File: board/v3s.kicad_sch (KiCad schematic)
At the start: 0 parts

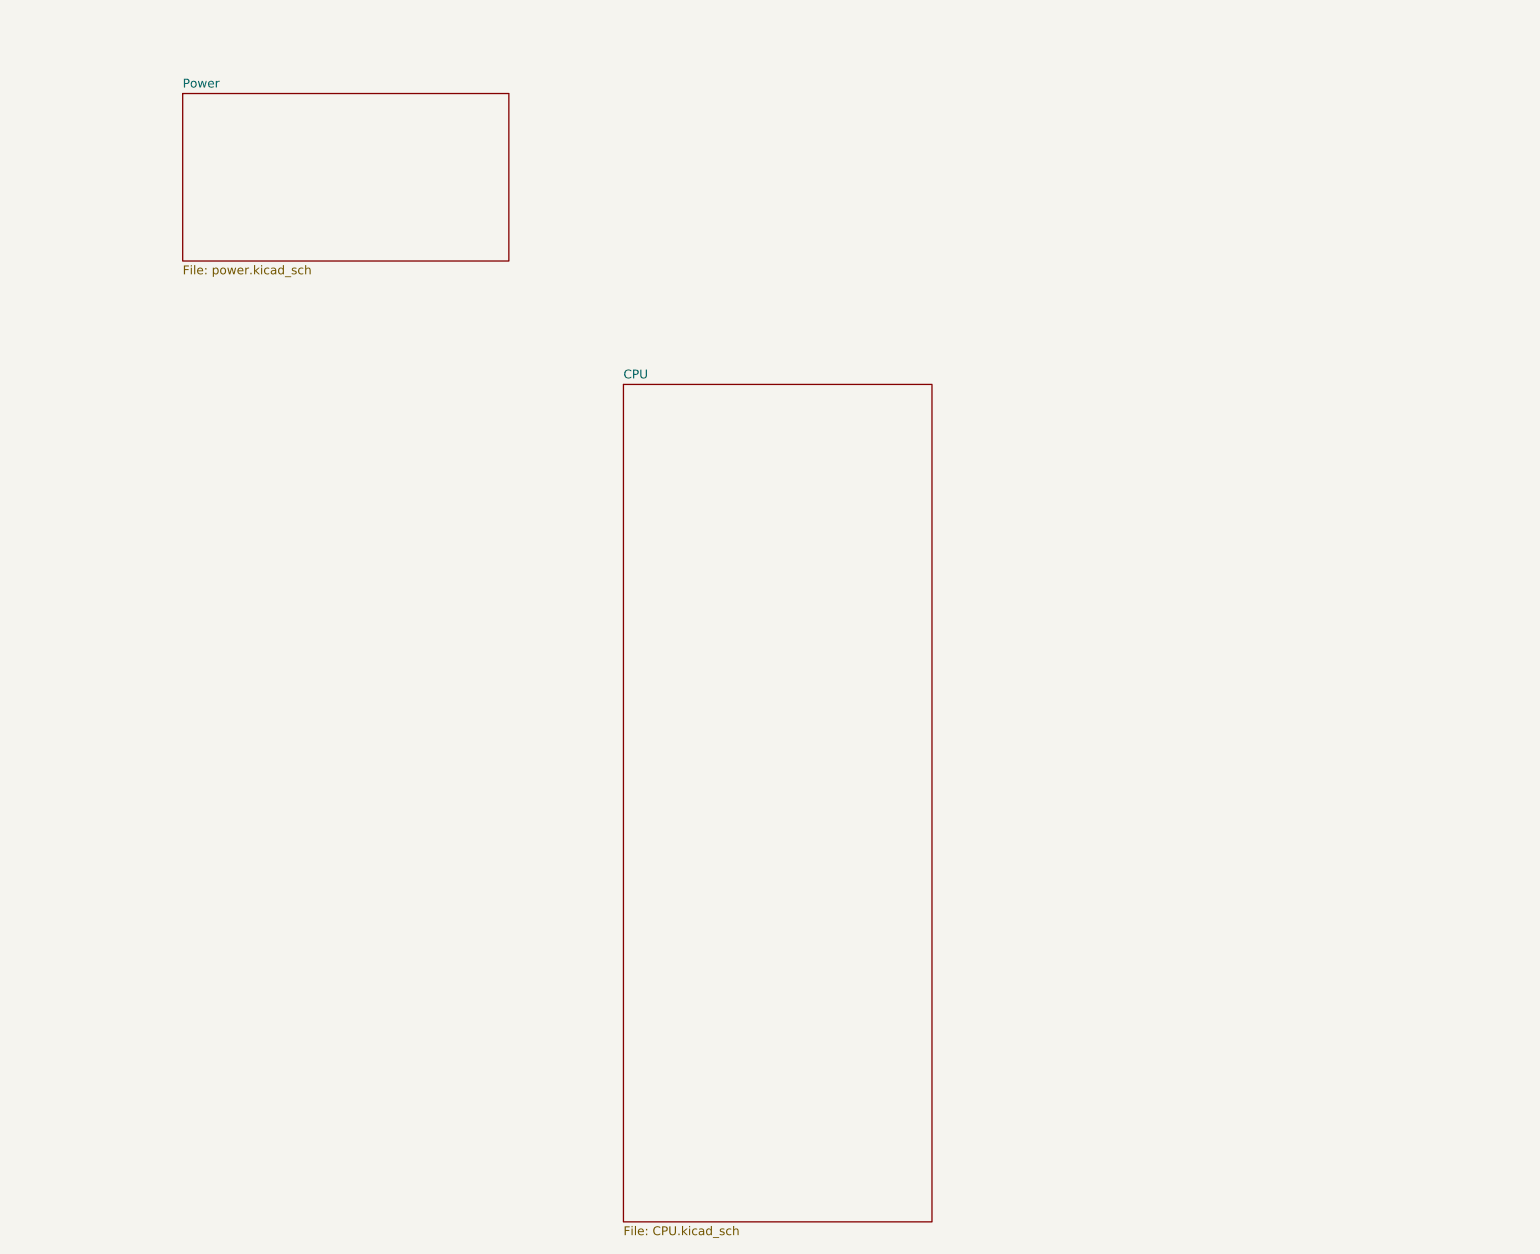
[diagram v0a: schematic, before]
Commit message: schematic update, choose components, creeate footprints
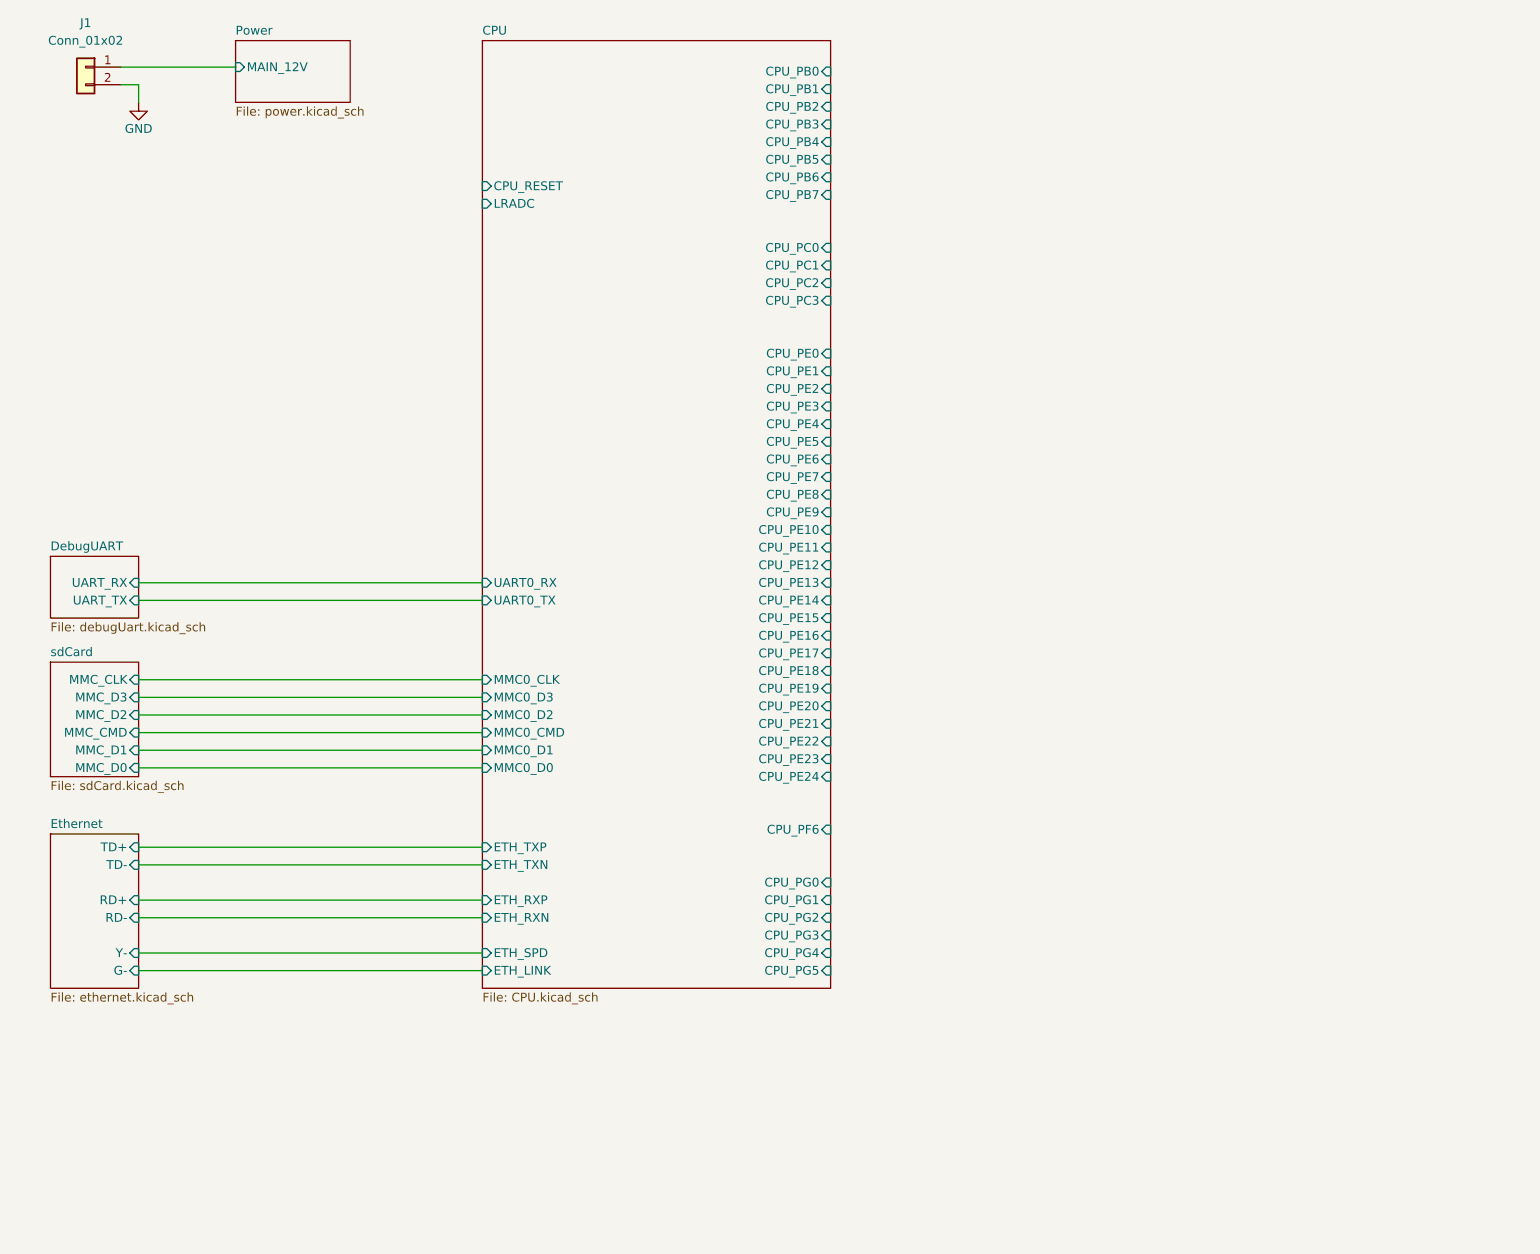
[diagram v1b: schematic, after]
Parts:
- added J1: Conn_01x02, Connector_JST:JST_PH_B2B-PH-K_1x02_P2.00mm_Vertical, symbol Connector_Generic:Conn_01x02
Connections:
- new net GND: J1.2 (Pin_2)
- new net Power/MAIN_12V: J1.1 (Pin_1)
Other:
- added sheet DebugUART (debugUart.kicad_sch)
- added sheet Ethernet (ethernet.kicad_sch)
- added sheet sdCard (sdCard.kicad_sch)
- sheet CPU ports: added CPU_PB0, CPU_PB1, CPU_PB2, CPU_PB3, CPU_PB4, CPU_PB5, CPU_PB6, CPU_PB7, CPU_PC0, CPU_PC1, CPU_PC2, CPU_PC3, CPU_PE0, CPU_PE1, CPU_PE10, CPU_PE11, CPU_PE12, CPU_PE13, CPU_PE14, CPU_PE15, CPU_PE16, CPU_PE17, CPU_PE18, CPU_PE19, CPU_PE2, CPU_PE20, CPU_PE21, CPU_PE22, CPU_PE23, CPU_PE24, CPU_PE3, CPU_PE4, CPU_PE5, CPU_PE6, CPU_PE7, CPU_PE8, CPU_PE9, CPU_PF6, CPU_PG0, CPU_PG1, CPU_PG2, CPU_PG3, CPU_PG4, CPU_PG5, CPU_RESET, ETH_LINK, ETH_RXN, ETH_RXP, ETH_SPD, ETH_TXN, ETH_TXP, LRADC, MMC0_CLK, MMC0_CMD, MMC0_D0, MMC0_D1, MMC0_D2, MMC0_D3, UART0_RX, UART0_TX; removed none
- sheet Power ports: added MAIN_12V; removed none

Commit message: pcb layout
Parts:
- added J3: Conn_02x13_Odd_Even, Connector_PinHeader_2.54mm:PinHeader_2x13_P2.54mm_Vertical, symbol Connector_Generic:Conn_02x13_Odd_Even
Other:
- sheet CPU ports: added USB_DN, USB_DP; removed none

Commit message: update layout
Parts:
- added J4: Conn_01x02, Connector_PinHeader_2.54mm:PinHeader_1x02_P2.54mm_Vertical, symbol Connector_Generic:Conn_01x02
- added J5: Conn_02x13_Odd_Even, Connector_PinHeader_2.54mm:PinHeader_2x13_P2.54mm_Vertical, symbol Connector_Generic:Conn_02x13_Odd_Even
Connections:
- net CPU/CPU_RESET: now also J4.1 (Pin_1)
- net CPU_PE0: now also J3.1 (Pin_1)
- net CPU_PE1: now also J3.2 (Pin_2)
- net CPU_PE10: now also J3.11 (Pin_11)
- net CPU_PE11: now also J3.12 (Pin_12)
- net CPU_PE12: now also J3.13 (Pin_13)
- net CPU_PE13: now also J3.14 (Pin_14)
- net CPU_PE14: now also J3.15 (Pin_15)
- net CPU_PE15: now also J3.16 (Pin_16)
- net CPU_PE16: now also J3.17 (Pin_17)
- net CPU_PE17: now also J3.18 (Pin_18)
- net CPU_PE18: now also J3.19 (Pin_19)
- net CPU_PE19: now also J3.20 (Pin_20)
- net CPU_PE2: now also J3.3 (Pin_3)
- net CPU_PE20: now also J3.21 (Pin_21)
- net CPU_PE21: now also J3.22 (Pin_22)
- net CPU_PE22: now also J3.23 (Pin_23)
- net CPU_PE23: now also J3.24 (Pin_24)
- net CPU_PE24: now also J3.25 (Pin_25)
- net CPU_PE3: now also J3.4 (Pin_4)
- net CPU_PE4: now also J3.5 (Pin_5)
- net CPU_PE5: now also J3.6 (Pin_6)
- net CPU_PE6: now also J3.7 (Pin_7)
- net CPU_PE7: now also J3.8 (Pin_8)
- net CPU_PE8: now also J3.9 (Pin_9)
- net CPU_PE9: now also J3.10 (Pin_10)
- net GND: now also J3.26 (Pin_26), J4.2 (Pin_2), J5.17 (Pin_17), J5.18 (Pin_18), J5.25 (Pin_25), J5.26 (Pin_26), J5.7 (Pin_7), J5.8 (Pin_8)
- new net +3V3: J5.1 (Pin_1), J5.2 (Pin_2)
- new net CPU_PB0: J5.16 (Pin_16)
- new net CPU_PB1: J5.15 (Pin_15)
- new net CPU_PB2: J5.14 (Pin_14)
- new net CPU_PB3: J5.13 (Pin_13)
- new net CPU_PB4: J5.12 (Pin_12)
- new net CPU_PB5: J5.11 (Pin_11)
- new net CPU_PB6: J5.10 (Pin_10)
- new net CPU_PB7: J5.9 (Pin_9)
- new net CPU_PC0: J5.6 (Pin_6)
- new net CPU_PC1: J5.5 (Pin_5)
- new net CPU_PC2: J5.4 (Pin_4)
- new net CPU_PC3: J5.3 (Pin_3)
- new net CPU_PG0: J5.20 (Pin_20)
- new net CPU_PG1: J5.19 (Pin_19)
- new net CPU_PG2: J5.22 (Pin_22)
- new net CPU_PG3: J5.21 (Pin_21)
- new net CPU_PG4: J5.24 (Pin_24)
- new net CPU_PG5: J5.23 (Pin_23)
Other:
- sheet CPU ports: added none; removed LRADC
- moved on the sheet: J3

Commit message: updates, finish layout, remove usb-uart
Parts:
- added D1: D_Small, Diode_SMD:D_SMA, symbol Device:D_Small
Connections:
- net Power/MAIN_12V: now also D1.1 (K); no longer J1.1 (Pin_1)
- new net: D1.2 (A), J1.1 (Pin_1)
